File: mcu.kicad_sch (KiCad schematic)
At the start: 16 parts, among them U3 STM32F072CxUx, Y1 ECS-160-10-37-RWM-TR

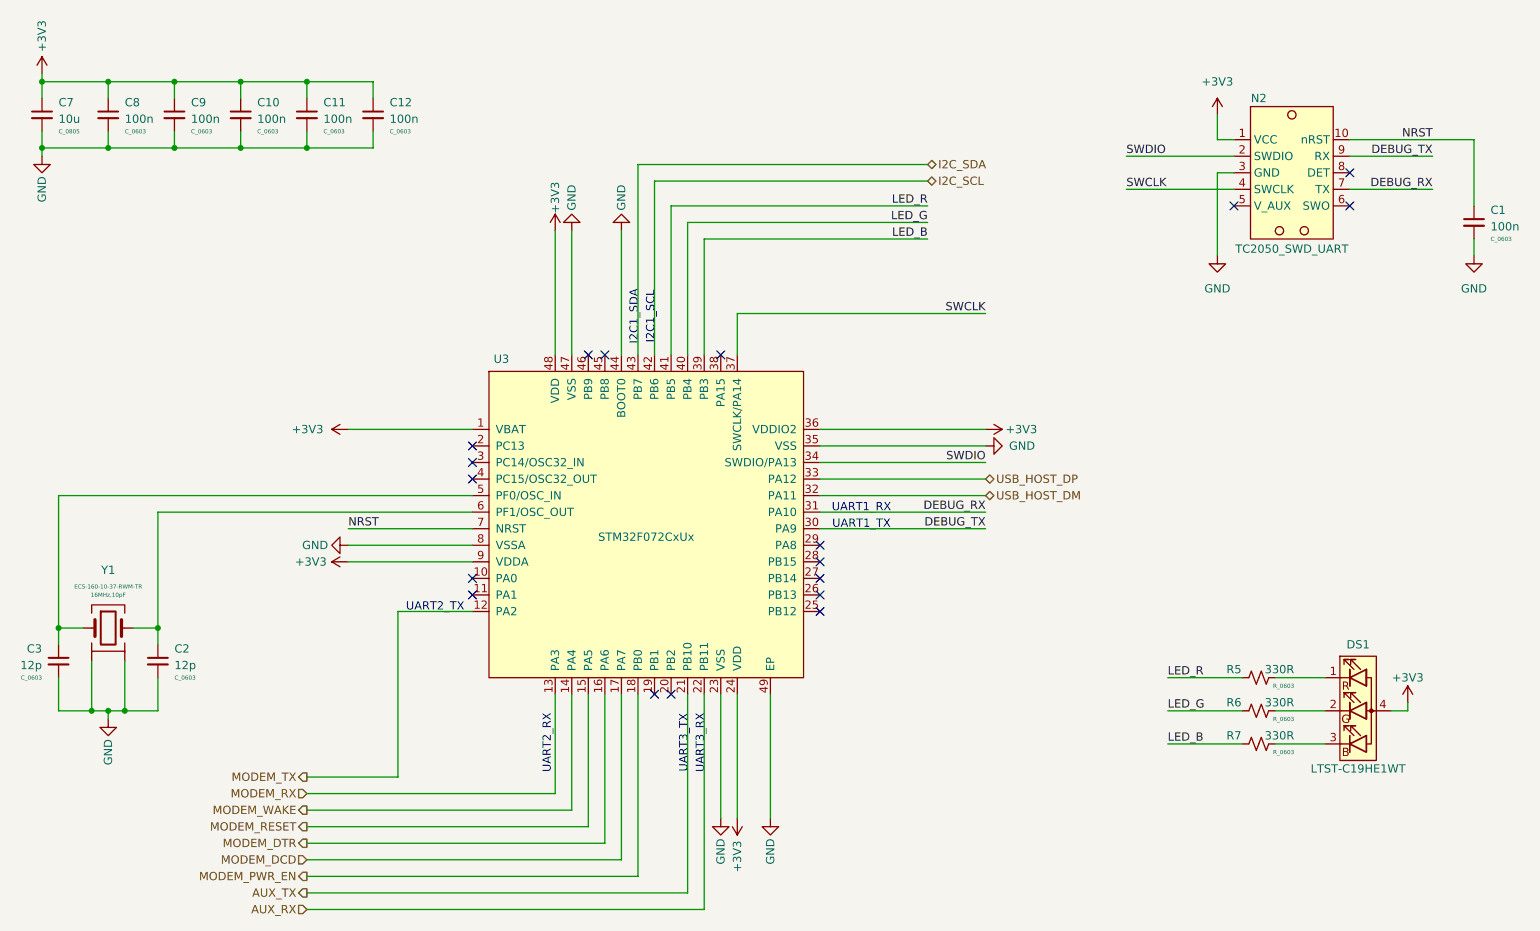
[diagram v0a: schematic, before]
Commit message: Reannotate components
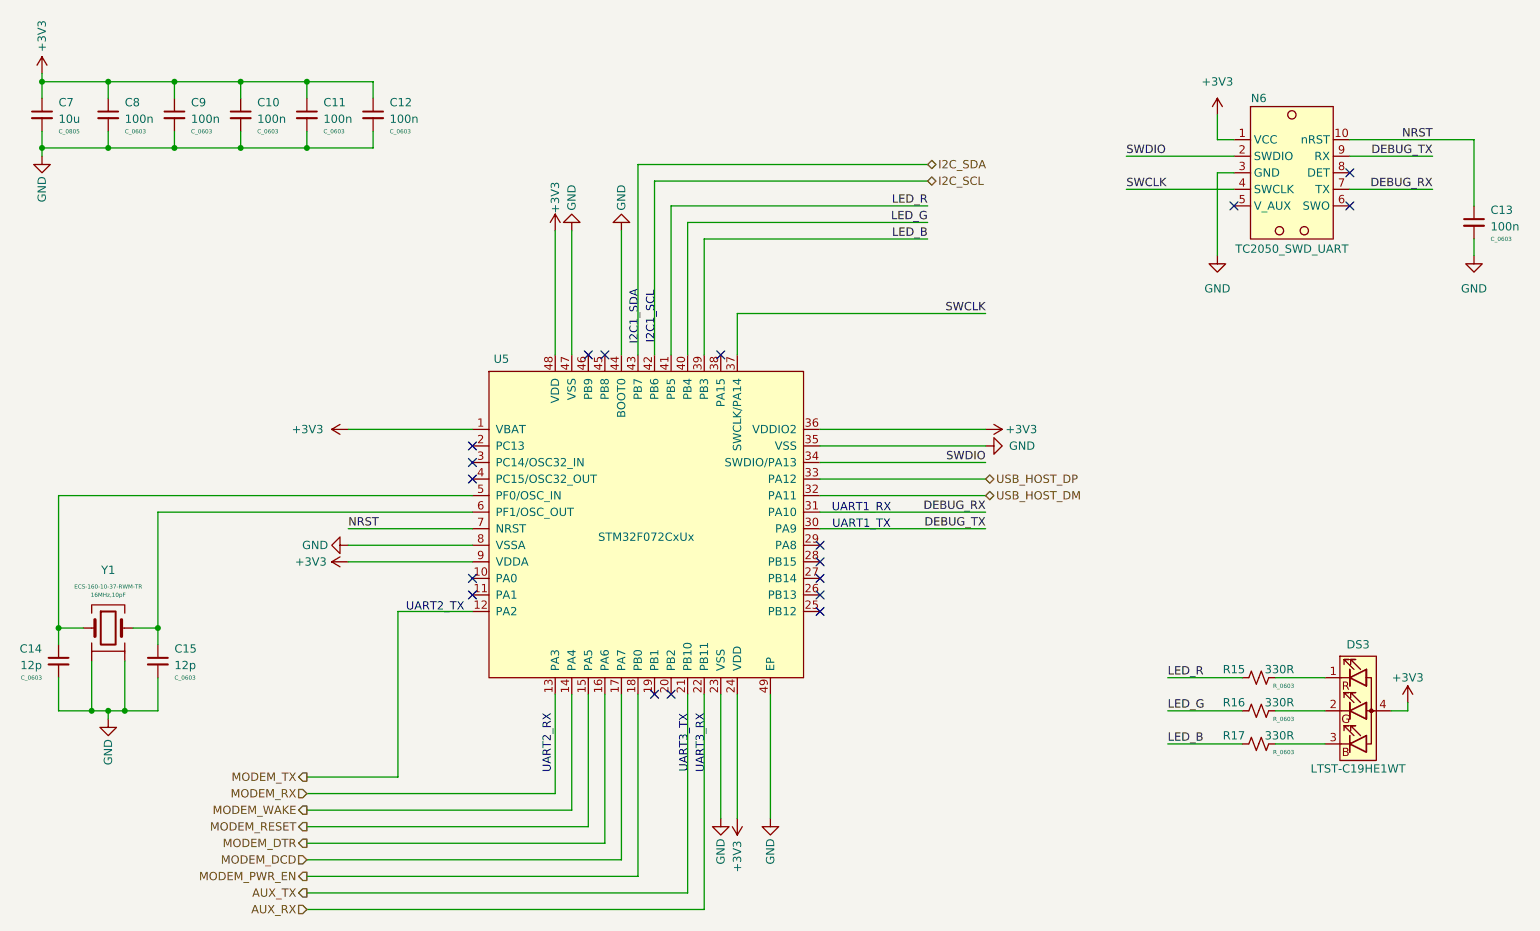
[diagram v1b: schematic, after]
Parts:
- renumbered C1 to C13, C3 to C14, C2 to C15, DS1 to DS3, N2 to N6, R5 to R15, R6 to R16, R7 to R17, U3 to U5
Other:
- company: (none) -> TL Embedded
- title: (none) -> Winglet Carrier Board
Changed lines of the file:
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@@
 	(generator_version "8.0")
 	(paper "A4")
+	(title_block
+		(title "Winglet Carrier Board")
+		(date "2024-08-09")
+		(rev "v1.0")
+		(company "TL Embedded")
+	)
 	(junction
 		(at 43.18 134.62)
@@
 		(on_board yes)
 		(dnp no)
-		(property "Reference" "R6"
+		(property "Reference" "R16"
 			(at 215.9 133.35 90)
 			(effects
@@
 			(project "Winglet-Carrier"
 				(path "/bbb905ef-a222-43ea-83e2-d1132f7d94bb/6fc44d7f-b41f-4ce5-97e7-45ff3882061f"
-					(reference "R6")
+					(reference "R16")
 					(unit 1)
 				)
@@
 		(on_board yes)
 		(dnp no)
-		(property "Reference" "#PWR030"
+		(property "Reference" "#PWR015"
 			(at 33.02 40.64 0)
 			(effects
@@
 			(project "Winglet-Carrier"
 				(path "/bbb905ef-a222-43ea-83e2-d1132f7d94bb/6fc44d7f-b41f-4ce5-97e7-45ff3882061f"
-					(reference "#PWR030")
+					(reference "#PWR015")
 					(unit 1)
 				)
@@
 		(on_board yes)
 		(dnp no)
-		(property "Reference" "#PWR017"
+		(property "Reference" "#PWR032"
 			(at 144.78 157.48 0)
 			(effects
@@
 			(project "Winglet-Carrier"
 				(path "/bbb905ef-a222-43ea-83e2-d1132f7d94bb/6fc44d7f-b41f-4ce5-97e7-45ff3882061f"
-					(reference "#PWR017")
+					(reference "#PWR032")
 					(unit 1)
 				)
@@
 		(on_board yes)
 		(dnp no)
-		(property "Reference" "#PWR018"
+		(property "Reference" "#PWR026"
 			(at 73.66 109.22 0)
 			(effects
@@
 			(project "Winglet-Carrier"
 				(path "/bbb905ef-a222-43ea-83e2-d1132f7d94bb/6fc44d7f-b41f-4ce5-97e7-45ff3882061f"
-					(reference "#PWR018")
+					(reference "#PWR026")
 					(unit 1)
 				)
@@
 		(dnp no)
 		(fields_autoplaced yes)
-		(property "Reference" "#PWR011"
+		(property "Reference" "#PWR016"
 			(at 213.36 46.99 0)
 			(effects
@@
 			(project ""
 				(path "/bbb905ef-a222-43ea-83e2-d1132f7d94bb/6fc44d7f-b41f-4ce5-97e7-45ff3882061f"
-					(reference "#PWR011")
+					(reference "#PWR016")
 					(unit 1)
 				)
@@
 		(dnp no)
 		(fields_autoplaced yes)
-		(property "Reference" "#PWR012"
+		(property "Reference" "#PWR021"
 			(at 213.36 71.12 0)
 			(effects
@@
 			(project "Winglet-Carrier"
 				(path "/bbb905ef-a222-43ea-83e2-d1132f7d94bb/6fc44d7f-b41f-4ce5-97e7-45ff3882061f"
-					(reference "#PWR012")
+					(reference "#PWR021")
 					(unit 1)
 				)
@@
 		(on_board yes)
 		(dnp no)
-		(property "Reference" "DS1"
+		(property "Reference" "DS3"
 			(at 234.95 124.46 0)
 			(effects
@@
 			(project ""
 				(path "/bbb905ef-a222-43ea-83e2-d1132f7d94bb/6fc44d7f-b41f-4ce5-97e7-45ff3882061f"
-					(reference "DS1")
+					(reference "DS3")
 					(unit 1)
 				)
@@
 		(dnp no)
 		(fields_autoplaced yes)
-		(property "Reference" "#PWR024"
+		(property "Reference" "#PWR022"
 			(at 252.73 71.12 0)
 			(effects
@@
 			(project "Winglet-Carrier"
 				(path "/bbb905ef-a222-43ea-83e2-d1132f7d94bb/6fc44d7f-b41f-4ce5-97e7-45ff3882061f"
-					(reference "#PWR024")
+					(reference "#PWR022")
 					(unit 1)
 				)
@@
 		(on_board yes)
 		(dnp no)
-		(property "Reference" "U3"
+		(property "Reference" "U5"
 			(at 103.505 80.645 0)
 			(effects
@@
 			(project ""
 				(path "/bbb905ef-a222-43ea-83e2-d1132f7d94bb/6fc44d7f-b41f-4ce5-97e7-45ff3882061f"
-					(reference "U3")
+					(reference "U5")
 					(unit 1)
 				)
@@
 		(on_board yes)
 		(dnp no)
-		(property "Reference" "#PWR022"
+		(property "Reference" "#PWR031"
 			(at 139.7 147.32 0)
 			(effects
@@
 			(project "Winglet-Carrier"
 				(path "/bbb905ef-a222-43ea-83e2-d1132f7d94bb/6fc44d7f-b41f-4ce5-97e7-45ff3882061f"
-					(reference "#PWR022")
+					(reference "#PWR031")
 					(unit 1)
 				)
@@
 		(on_board yes)
 		(dnp no)
-		(property "Reference" "#PWR016"
+		(property "Reference" "#PWR030"
 			(at 137.16 157.48 0)
 			(effects
@@
 			(project "Winglet-Carrier"
 				(path "/bbb905ef-a222-43ea-83e2-d1132f7d94bb/6fc44d7f-b41f-4ce5-97e7-45ff3882061f"
-					(reference "#PWR016")
+					(reference "#PWR030")
 					(unit 1)
 				)
@@
 		(on_board yes)
 		(dnp no)
-		(property "Reference" "R7"
+		(property "Reference" "R17"
 			(at 215.9 138.43 90)
 			(effects
@@
 			(project "Winglet-Carrier"
 				(path "/bbb905ef-a222-43ea-83e2-d1132f7d94bb/6fc44d7f-b41f-4ce5-97e7-45ff3882061f"
-					(reference "R7")
+					(reference "R17")
 					(unit 1)
 				)
@@
 		(dnp no)
 		(fields_autoplaced yes)
-		(property "Reference" "C3"
+		(property "Reference" "C14"
 			(at 33.02 125.1012 0)
 			(effects
@@
 			(project "Winglet-Carrier"
 				(path "/bbb905ef-a222-43ea-83e2-d1132f7d94bb/6fc44d7f-b41f-4ce5-97e7-45ff3882061f"
-					(reference "C3")
+					(reference "C14")
 					(unit 1)
 				)
@@
 		(on_board yes)
 		(dnp no)
-		(property "Reference" "#PWR025"
+		(property "Reference" "#PWR028"
 			(at 242.57 137.16 0)
 			(effects
@@
 			(project "Winglet-Carrier"
 				(path "/bbb905ef-a222-43ea-83e2-d1132f7d94bb/6fc44d7f-b41f-4ce5-97e7-45ff3882061f"
-					(reference "#PWR025")
+					(reference "#PWR028")
 					(unit 1)
 				)
@@
 		(on_board yes)
 		(dnp no)
-		(property "Reference" "#PWR020"
+		(property "Reference" "#PWR018"
 			(at 111.76 64.77 0)
 			(effects
@@
 			(project "Winglet-Carrier"
 				(path "/bbb905ef-a222-43ea-83e2-d1132f7d94bb/6fc44d7f-b41f-4ce5-97e7-45ff3882061f"
-					(reference "#PWR020")
+					(reference "#PWR018")
 					(unit 1)
 				)
@@
 		(on_board yes)
 		(dnp no)
-		(property "Reference" "R5"
+		(property "Reference" "R15"
 			(at 215.9 128.27 90)
 			(effects
@@
 			(project ""
 				(path "/bbb905ef-a222-43ea-83e2-d1132f7d94bb/6fc44d7f-b41f-4ce5-97e7-45ff3882061f"
-					(reference "R5")
+					(reference "R15")
 					(unit 1)
 				)
@@
 		(on_board yes)
 		(dnp no)
-		(property "Reference" "#PWR021"
+		(property "Reference" "#PWR024"
 			(at 173.99 91.44 0)
 			(effects
@@
 			(project "Winglet-Carrier"
 				(path "/bbb905ef-a222-43ea-83e2-d1132f7d94bb/6fc44d7f-b41f-4ce5-97e7-45ff3882061f"
-					(reference "#PWR021")
+					(reference "#PWR024")
 					(unit 1)
 				)
@@
 		(on_board yes)
 		(dnp no)
-		(property "Reference" "N2"
+		(property "Reference" "N6"
 			(at 219.71 40.64 0)
 			(effects
@@
 			(project ""
 				(path "/bbb905ef-a222-43ea-83e2-d1132f7d94bb/6fc44d7f-b41f-4ce5-97e7-45ff3882061f"
-					(reference "N2")
+					(reference "N6")
 					(unit 1)
 				)
@@
 		(on_board yes)
 		(dnp no)
-		(property "Reference" "#PWR029"
+		(property "Reference" "#PWR017"
 			(at 33.02 55.88 0)
 			(effects
@@
 			(project "Winglet-Carrier"
 				(path "/bbb905ef-a222-43ea-83e2-d1132f7d94bb/6fc44d7f-b41f-4ce5-97e7-45ff3882061f"
-					(reference "#PWR029")
+					(reference "#PWR017")
 					(unit 1)
 				)
@@
 		(dnp no)
 		(fields_autoplaced yes)
-		(property "Reference" "C2"
+		(property "Reference" "C15"
 			(at 53.34 125.1012 0)
 			(effects
@@
 			(project ""
 				(path "/bbb905ef-a222-43ea-83e2-d1132f7d94bb/6fc44d7f-b41f-4ce5-97e7-45ff3882061f"
-					(reference "C2")
+					(reference "C15")
 					(unit 1)
 				)
@@
 		(on_board yes)
 		(dnp no)
-		(property "Reference" "#PWR015"
+		(property "Reference" "#PWR025"
 			(at 184.15 93.98 0)
 			(effects
@@
 			(project "Winglet-Carrier"
 				(path "/bbb905ef-a222-43ea-83e2-d1132f7d94bb/6fc44d7f-b41f-4ce5-97e7-45ff3882061f"
-					(reference "#PWR015")
+					(reference "#PWR025")
 					(unit 1)
 				)
@@
 		(on_board yes)
 		(dnp no)
-		(property "Reference" "#PWR026"
+		(property "Reference" "#PWR029"
 			(at 43.18 142.24 0)
 			(effects
@@
 			(project "Winglet-Carrier"
 				(path "/bbb905ef-a222-43ea-83e2-d1132f7d94bb/6fc44d7f-b41f-4ce5-97e7-45ff3882061f"
-					(reference "#PWR026")
+					(reference "#PWR029")
 					(unit 1)
 				)
@@
 		(on_board yes)
 		(dnp no)
-		(property "Reference" "#PWR019"
+		(property "Reference" "#PWR027"
 			(at 83.82 111.76 0)
 			(effects
@@
 			(project "Winglet-Carrier"
 				(path "/bbb905ef-a222-43ea-83e2-d1132f7d94bb/6fc44d7f-b41f-4ce5-97e7-45ff3882061f"
-					(reference "#PWR019")
+					(reference "#PWR027")
 					(unit 1)
 				)
@@
 		(on_board yes)
 		(dnp no)
-		(property "Reference" "#PWR014"
+		(property "Reference" "#PWR019"
 			(at 114.3 54.61 0)
 			(effects
@@
 			(project "Winglet-Carrier"
 				(path "/bbb905ef-a222-43ea-83e2-d1132f7d94bb/6fc44d7f-b41f-4ce5-97e7-45ff3882061f"
-					(reference "#PWR014")
+					(reference "#PWR019")
 					(unit 1)
 				)
@@
 		(on_board yes)
 		(dnp no)
-		(property "Reference" "#PWR013"
+		(property "Reference" "#PWR020"
 			(at 121.92 54.61 0)
 			(effects
@@
 			(project "Winglet-Carrier"
 				(path "/bbb905ef-a222-43ea-83e2-d1132f7d94bb/6fc44d7f-b41f-4ce5-97e7-45ff3882061f"
-					(reference "#PWR013")
+					(reference "#PWR020")
 					(unit 1)
 				)
@@
 		(dnp no)
 		(fields_autoplaced yes)
-		(property "Reference" "C1"
+		(property "Reference" "C13"
 			(at 255.27 57.7912 0)
 			(effects
@@
 			(project ""
 				(path "/bbb905ef-a222-43ea-83e2-d1132f7d94bb/6fc44d7f-b41f-4ce5-97e7-45ff3882061f"
-					(reference "C1")
+					(reference "C13")
 					(unit 1)
 				)
